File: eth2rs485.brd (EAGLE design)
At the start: 31.7 x 86.4 mm, 64 parts, among them IC1 VREG-OKI-78SR-5.0/1.5-W36, IC2 MAX485, IC3 24AA025E48, Q1 16MHz, T1 74990101217, U1 AP2210K, U2 ATMEGA328P-AU, U3 W5500, Y1 IT-L30-010

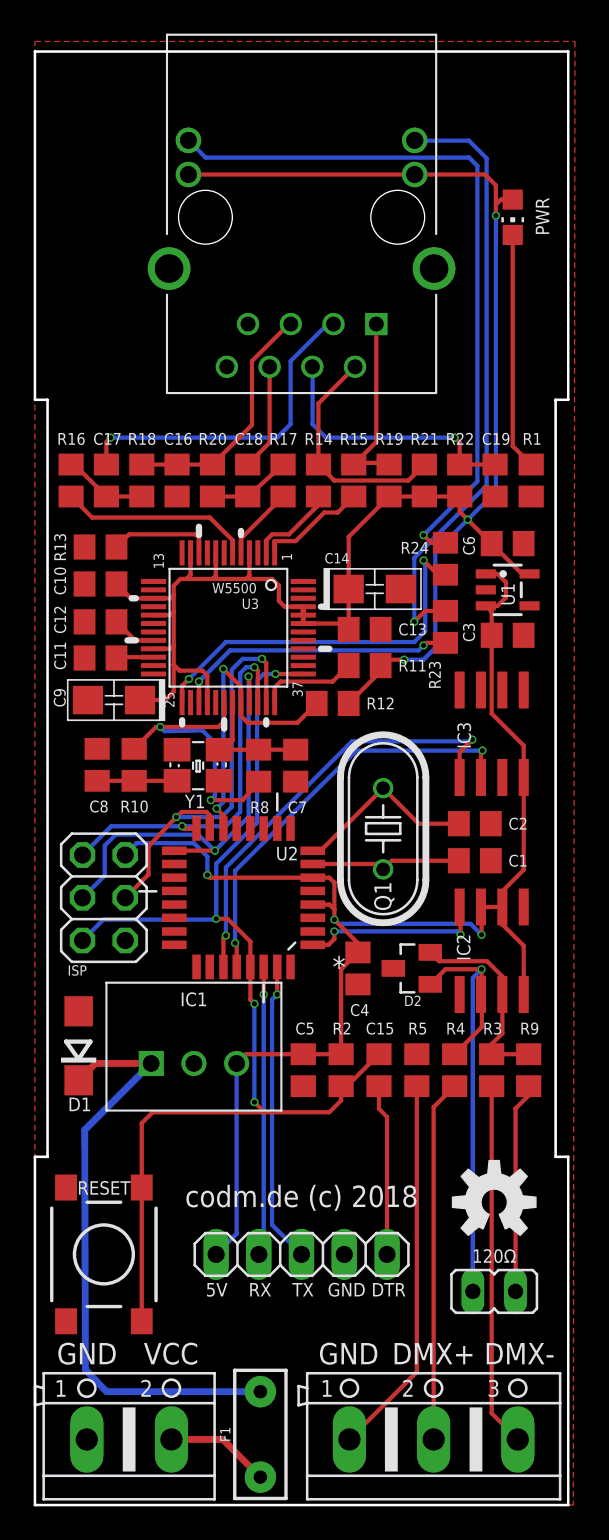
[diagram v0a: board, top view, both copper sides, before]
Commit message: swapped 328p for 644p
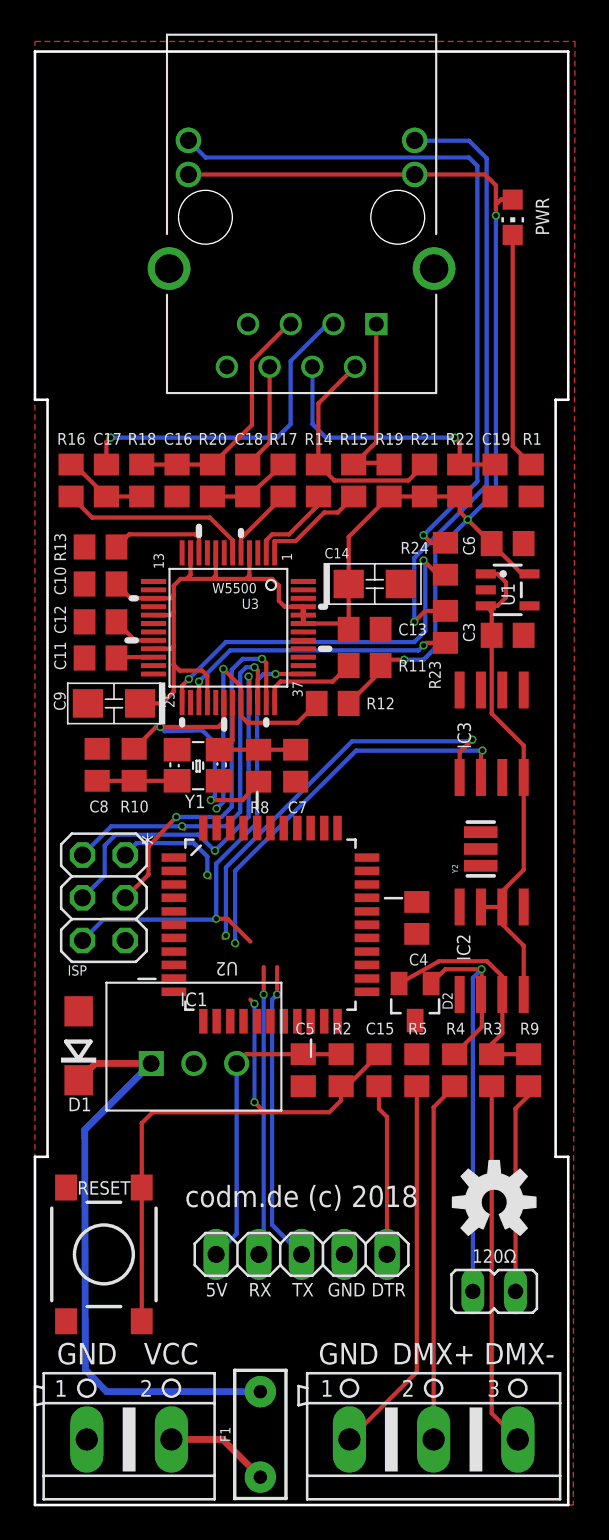
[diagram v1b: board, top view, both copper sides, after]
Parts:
- removed C1, C2: 22pF, rcl:C0805
- removed Q1: 16MHz, adafruit:HC49U70
- added Y2: CSTCE16M0V53-R0 16MHZ, SmartPrj:RESONATOR
- U2: value ATMEGA328P-AU -> ATMEGA644P-20AU; device Atmel_By_element14_Batch_1-00:QFP80P900X900X120-32N -> Atmel_By_element14_Batch_1-00:QFP80P1200X1200X120-44N
- moved C4 4.61 mm to (22.7, 34.9)
- moved U2 2.26 mm to (14.0, 34.5), turned to 0 degrees
- moved D2 2.01 mm to (22.6, 29.9), turned to 180 degrees
- moved C14 0.30 mm to (20.2, 54.8)
- moved C9 0.20 mm to (4.70, 47.6)
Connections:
- removed net DOUT: IC2.4, U2.1
- new net RXD0: U2.9
- new net TXD0: U2.10
- net +5V: now also U2.17, U2.38, U2.5; no longer U2.4, U2.6
- net AVCC: now also U2.27; no longer U2.18
- net GND: now also U2.18, U2.28, U2.39, U2.6, Y2.2; no longer C1.1, C2.1, U2.21, U2.3, U2.5
- net MISO: now also U2.2; no longer U2.16
- net MOSI: now also U2.1; no longer U2.15
- net N$2: now also Y2.3; no longer C2.2, Q1.1
- net N$3: now also Y2.1; no longer C1.2, Q1.2
- net RST: no longer U2.29
- net RXD: no longer U2.30
- net SCL: now also U2.19; no longer U2.28
- net SCLK: now also U2.3; no longer U2.17
- net SCSN: now also U2.44; no longer U2.14
- net SDA: now also U2.20; no longer U2.27
- net TXD: no longer U2.31
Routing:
- net +5V: track 86.1 -> 55.2 mm, vias 3 -> 1
- net DOUT: track 11.1 -> 0.00 mm, vias 2 -> 0
- net N$2: track 11.1 -> 0.00 mm
- net N$3: track 9.03 -> 0.00 mm
- net RST: track 67.7 -> 64.2 mm
- net MOSI: track 25.5 -> 22.5 mm
- net SCLK: track 26.1 -> 23.6 mm
- net B: track 12.0 -> 13.9 mm
- net SDA: track 26.3 -> 24.6 mm
- net SCSN: track 18.9 -> 17.6 mm
- net SCL: track 25.1 -> 23.9 mm
- net MISO: track 22.8 -> 22.0 mm

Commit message: finished routing for prototype
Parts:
- removed R14, R15, R16, R17: 33R, rcl:R0805
- added R6: 10k, rcl:R0805
- U1: value AP2210K -> AP2112
- moved IC3 19.3 mm to (11.2, 35.0), turned to 270 degrees
- moved Y2 11.9 mm to (14.6, 39.8), turned to 270 degrees
- moved U2 11.6 mm to (23.2, 41.6)
- moved R23 10.9 mm to (17.9, 60.9)
- moved R24 9.86 mm to (15.7, 60.9)
- moved C9 9.50 mm to (4.60, 57.1)
- moved IC2 6.76 mm to (20.6, 31.5), turned to 270 degrees
- moved C4 4.96 mm to (27.4, 33.3), turned to 0 degrees
- moved D2 4.73 mm to (27.3, 30.4), turned to 90 degrees
- moved R13 4.28 mm to (2.25, 60.9), turned to 270 degrees
- moved R12 2.70 mm to (19.4, 49.8), turned to 180 degrees
- moved C14 2.41 mm to (20.4, 57.1)
- moved C13 2.01 mm to (19.4, 54.0)
- moved R11 2.01 mm to (19.4, 51.9), turned to 180 degrees
- moved C7 0.94 mm to (14.7, 44.5)
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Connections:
- net N$2 renamed XTAL1
- net N$3 renamed XTAL2
- removed net AVCC: U2.27
- removed net N$20: R16.2, U3.6
- removed net N$26: R17.2, U3.5
- removed net N$27: R14.2, U3.2
- removed net N$28: R15.2, U3.1
- removed net RXD: JP3.2
- removed net TXD: JP3.3
- new net 485MODE: IC2.2, IC2.3, U2.15
- new net N$2: R6.1, U1.3
- new net RXD1: IC2.1, U2.11
- new net TXD1: IC2.4, U2.12
- net +5V: now also R6.2, U2.27; no longer IC2.2, IC2.3, U1.3
- net RST: now also U2.4
- net RXD0: now also JP3.2
- net RXN: now also U3.5; no longer R17.1
- net RXP: now also U3.6; no longer R16.1
- net TXD0: now also JP3.3
- net TXN: now also U3.1; no longer R15.1
- net TXP: now also U3.2; no longer R14.1
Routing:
- net +5V: track 55.2 -> 99.9 mm, vias 1 -> 3
- net RXD0: track 0.00 -> 31.5 mm, vias 0 -> 1
- net TXD0: track 0.00 -> 31.3 mm, vias 0 -> 1
- net RST: track 64.2 -> 93.6 mm
- net TXD: track 17.9 -> 0.00 mm, vias 1 -> 0
- net RXD: track 17.2 -> 0.00 mm, vias 1 -> 0
- net MISO: track 22.0 -> 37.3 mm
- net N$35: track 42.6 -> 28.7 mm
- net MOSI: track 22.5 -> 36.1 mm
- net SCLK: track 23.6 -> 36.1 mm, vias 2 -> 3
- net +3V3: track 113.5 -> 101.2 mm, vias 3 -> 0
- net N$34: track 36.2 -> 24.6 mm
- net N$20: track 11.4 -> 0.00 mm
- net SCL: track 23.9 -> 13.9 mm
- net TXN: track 10.9 -> 20.2 mm, vias 0 -> 2
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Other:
- board text added: "(A) DMX+"
- board text added: "(B) DMX-"
- board text added: "90040-V0.1"
- board text added: "Ethernet RS485 Bridge V0.4"
- board text added: "codm.de 2019 CC-BY-SA"
- board text removed: "90030-V0.4"
- board text removed: "DMX+"
- board text removed: "DMX-"
- board text removed: "Ethernet DMX Bridge V0.4"
- board text removed: "codm.de 2018 CC-BY-SA"
